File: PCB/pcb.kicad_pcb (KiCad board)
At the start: 2 copper layers, 116 x 75 mm, 174 parts, among them J1 EXT POWER, J2 TRACK POWER, J3 RJ45, J4 RJ45, J5 FROG0-1, J6 FROG2-3, J7 FROG4-5, J8 FROG6-7, K1 G6SK-2, K2 G6SK-2, K3 G6SK-2, K4 G6SK-2, K5 G6SK-2, K6 G6SK-2, K7 G6SK-2, K8 G6SK-2, M1 Motor_Servo, M2 Motor_Servo, M3 Motor_Servo, M4 Motor_Servo, M5 Motor_Servo, M6 Motor_Servo, M7 Motor_Servo, M8 Motor_Servo, Q1 MMBT2222A, Q10 MMBT2222A, Q11 MMBT2222A, Q12 MMBT2222A, Q13 MMBT2222A, Q14 MMBT2222A, Q15 MMBT2222A, Q16 MMBT2222A, Q2 MMBT2222A, Q3 MMBT2222A, Q4 MMBT2222A, Q5 MMBT2222A, Q6 MMBT2222A, Q7 MMBT2222A, Q8 MMBT2222A, Q9 MMBT2222A, SW2 Factory Reset, SW3 User, U2 PCA9685PW, U3 MCP23017_SO, U4 AP63205WU, U5 AP2114-3.3, U6 LM358, U7 TJA1051T-3, U8 MOUDLE-SEEEDUINO-XIAO-ESP32S3

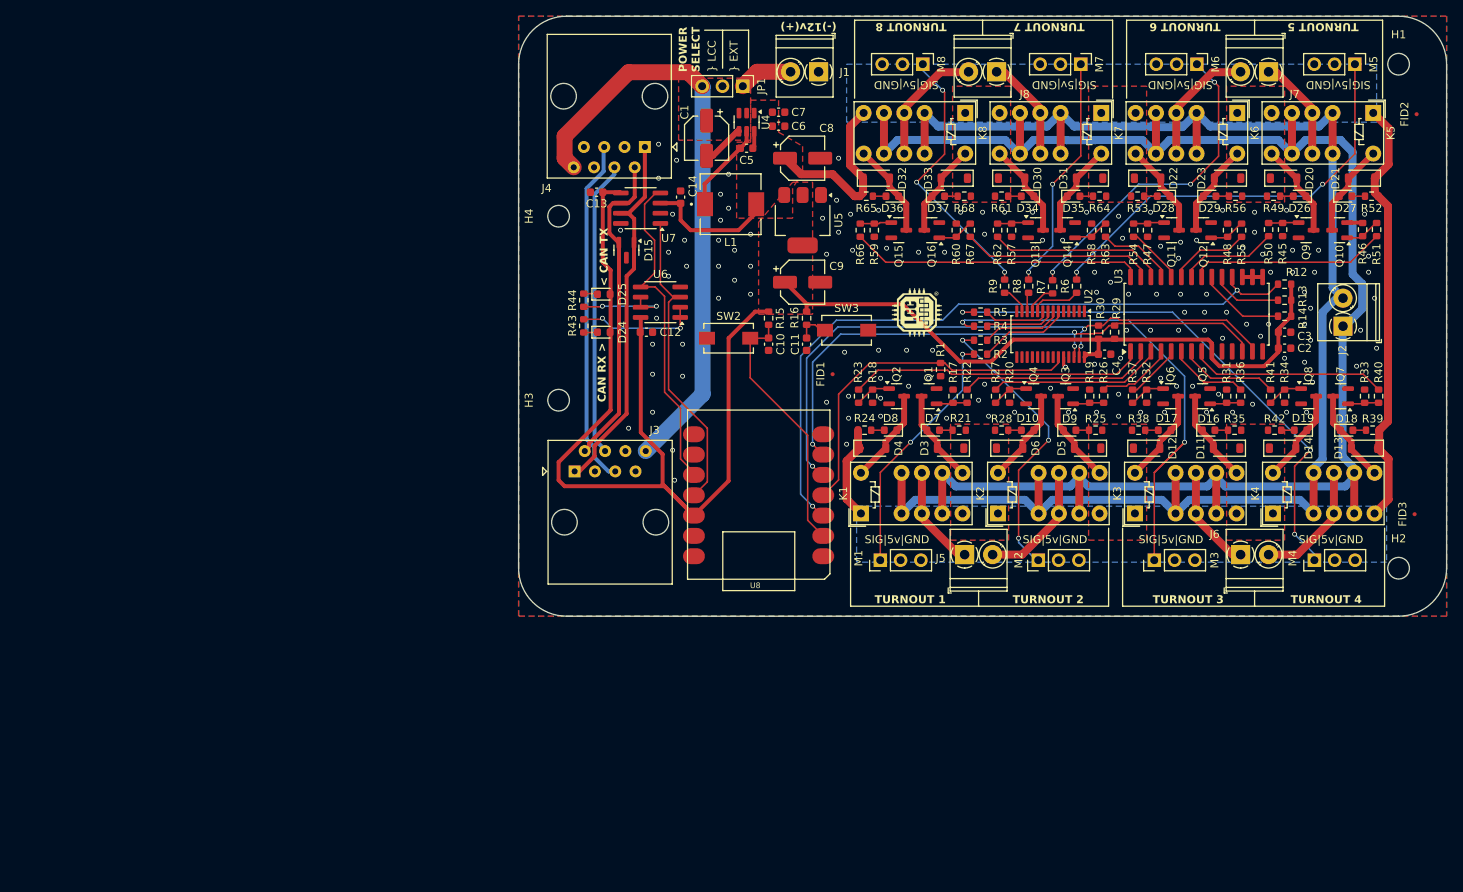
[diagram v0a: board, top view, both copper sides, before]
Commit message: Update with XIAO footprint
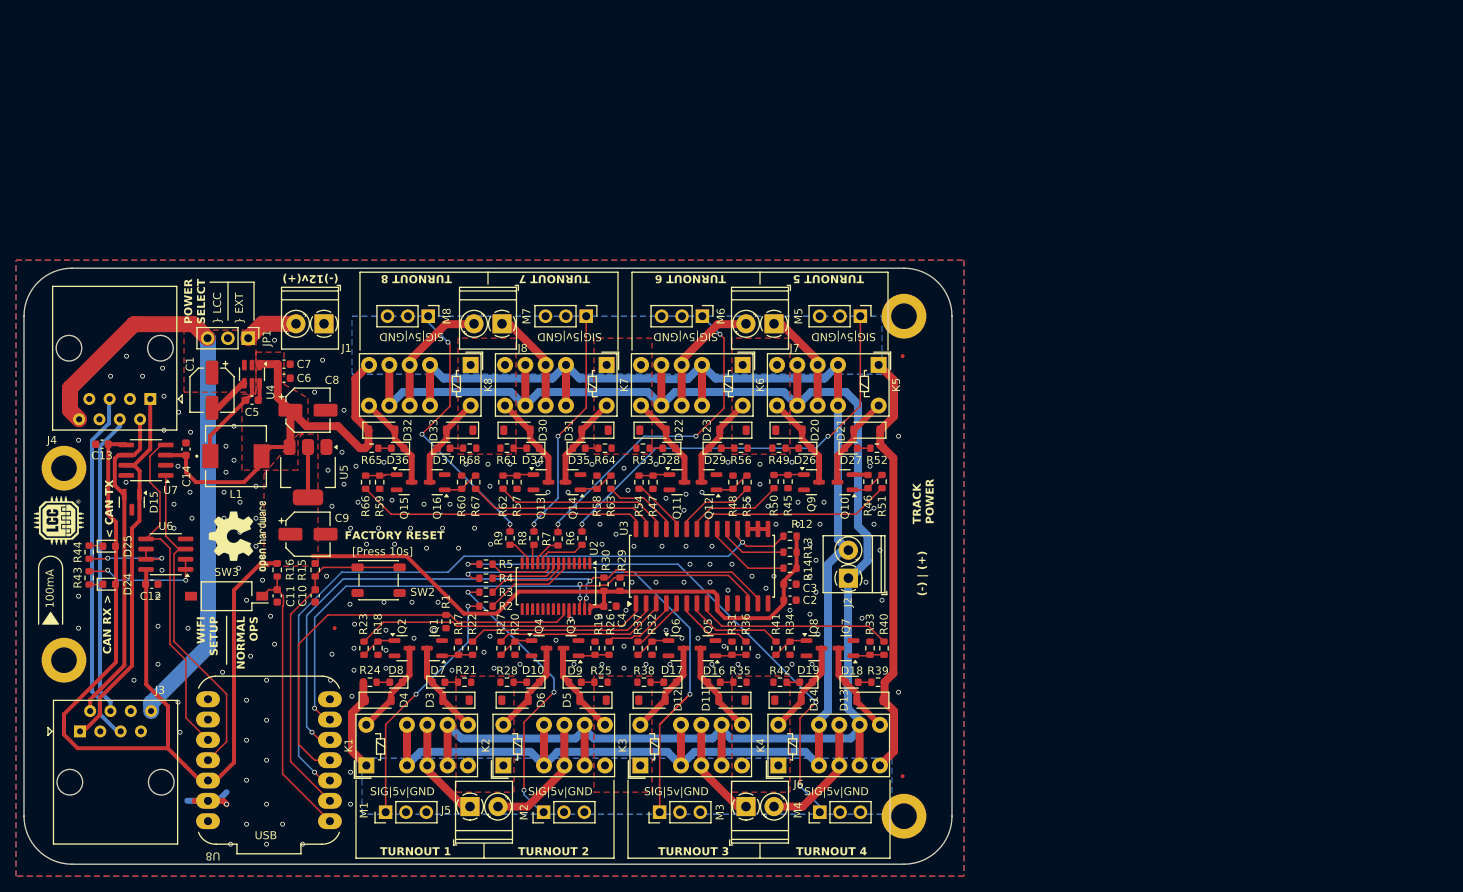
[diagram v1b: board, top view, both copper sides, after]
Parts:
- added REF**: OSHW-Logo2_9.8x8mm_SilkScreen, Symbol:OSHW-Logo2_9.8x8mm_SilkScreen, F.Cu at (106.0, 107.0)
- H1, H2, H3, H4: footprint MountingHole:MountingHole_2.7mm_M2.5 -> MountingHole:MountingHole_3.2mm_M3_DIN965_Pad
- SW2: footprint Button_Switch_SMD:SW_SPST_EVQPE1 -> Button_Switch_SMD:SW_SPST_PTS647_Sx50
- SW3: footprint Button_Switch_SMD:SW_SPST_EVQPE1 -> Button_Switch_SMD:SW_DIP_SPSTx01_Slide_Omron_A6S-110x_W8.9mm_P2.54mm
- U8: footprint xiao ESP32S3_PCB:MOUDLE14P-SMD-2.54-21X17.8MM -> CustomFootprints:MCU_Seeed_ESP32C3_TH
- moved G*** 110.4 mm to (83.5, 105.0)
- moved SW3 84.3 mm to (104.5, 114.5), turned to 180 degrees
- moved U8 82.6 mm to (109.8, 135.0)
- moved C11 73.3 mm to (110.8, 114.5)
- moved R16 73.3 mm to (110.8, 111.2)
- moved FID3 71.9 mm to (189.0, 137.0)
- moved FID2 71.0 mm to (189.0, 84.5)
- moved FID1 69.9 mm to (118.0, 118.5)
- moved H3 69.8 mm to (84.2, 122.5)
- moved J3 69.8 mm to (86.2, 131.4)
- moved D33 69.4 mm to (133.6, 93.8)
- moved D37 69.4 mm to (131.6, 96.0)
- moved J2 69.4 mm to (182.2, 112.2)
- moved K2 69.4 mm to (139.1, 135.7)
- moved K5 69.4 mm to (186.0, 85.6)
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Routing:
- net USER_BTN: track 4.26 -> 35.6 mm
- net +5V: track 106.2 -> 123.5 mm
- net FACTORY_RESET: track 32.2 -> 42.4 mm
- net GND: track 11.2 -> 20.7 mm, vias 136 -> 183
- net PWM_nENABLE: track 44.0 -> 53.4 mm
- net GPIO_nRESET: track 86.9 -> 89.8 mm
- net I2C_SDA: track 79.5 -> 82.4 mm
- net CAN-TX: track 39.3 -> 41.9 mm
- net I2C_SCL: track 73.2 -> 75.5 mm
- net CAN-RX: track 41.5 -> 43.5 mm
- net +3V3: track 202.1 -> 203.6 mm
- net ALT-A: track 37.0 -> 38.0 mm
- net VDDA: track 74.2 -> 75.2 mm
- net CAN-L: track 40.2 -> 41.2 mm
- net CAN-H: track 46.4 -> 47.3 mm
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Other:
- board size 116 x 75 mm -> 116 x 74.5 mm
- board text added: "(-) | (+)"
- board text added: "100mA"
- board text added: "FACTORY RESET"
- board text added: "NORMAL OPS"
- board text added: "TRACK POWER"
- board text added: "USB"
- board text added: "WIFI SETUP"
- board text added: "[Press 10s]"
- board text added: "https://github.com/vsi5004/LCCTurnoutController"

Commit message: Update project files
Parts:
- added D1: WiFi, LED_SMD:LED_0603_1608Metric, F.Cu at (107.8, 120.0)
- added D2: Activity, LED_SMD:LED_0603_1608Metric, F.Cu at (103.8, 120.0)
- added R10: 220R, Resistor_SMD:R_0603_1608Metric, F.Cu at (108.5, 122.5)
- added R11: 220R, Resistor_SMD:R_0603_1608Metric, F.Cu at (103.0, 122.5)
- H1, H2, H3, H4: footprint MountingHole:MountingHole_3.2mm_M3_DIN965_Pad -> MountingHole:MountingHole_3.2mm_M3_Pad
- SW2: footprint Button_Switch_SMD:SW_SPST_PTS647_Sx50 -> Button_Switch_SMD:SW_Tactile_SPST_NO_Straight_CK_PTS636Sx25SMTRLFS
- SW3: footprint Button_Switch_SMD:SW_DIP_SPSTx01_Slide_Omron_A6S-110x_W8.9mm_P2.54mm -> Button_Switch_SMD:SW_Tactile_SPST_NO_Straight_CK_PTS636Sx25SMTRLFS
- moved G*** 0.79 mm to (83.2, 105.8)
- moved SW2 0.79 mm to (122.8, 112.2)
- moved H3 0.72 mm to (83.5, 122.8)
- moved H4 0.67 mm to (83.5, 98.5)
- moved SW3 0.25 mm to (104.2, 114.5)
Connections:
- U8 pad 1: USER_BTN -> WIFI_LED
- U8 pad 10: CAN-RX -> CAN-TX
- U8 pad 11: CAN-TX -> ACTIVITY_LED
- U8 pad 2: FACTORY_RESET -> USER_BTN
- U8 pad 3: GPIO_nRESET -> FACTORY_RESET
- U8 pad 9: unconnected-(U8-PA7_A8_D8_SCK-Pad9) -> CAN-RX
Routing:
- net GPIO_nRESET: track 89.8 -> 8.59 mm, vias 2 -> 0
- net WIFI_LED: track 0.00 -> 23.6 mm
- net ACTIVITY_LED: track 0.00 -> 13.7 mm
- net FACTORY_RESET: track 42.4 -> 33.4 mm
- net +3V3: track 203.6 -> 206.1 mm
- net CAN-TX: track 41.9 -> 39.6 mm
- net CAN-RX: track 43.5 -> 41.6 mm
- net Net-(D2-K): track 0.00 -> 1.69 mm
- net Net-(D1-K): track 0.00 -> 1.69 mm
- net USER_BTN: track 35.6 -> 34.3 mm
- net I2C_SCL: track 75.5 -> 75.7 mm, vias 3 -> 2
- net I2C_SDA: vias 3 -> 2
- net GND: vias 183 -> 215
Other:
- board text added: "<WiFi"
- board text added: "Activity>"
- board text added: "USER"
- board text removed: "NORMAL OPS"
- board text removed: "WIFI SETUP"

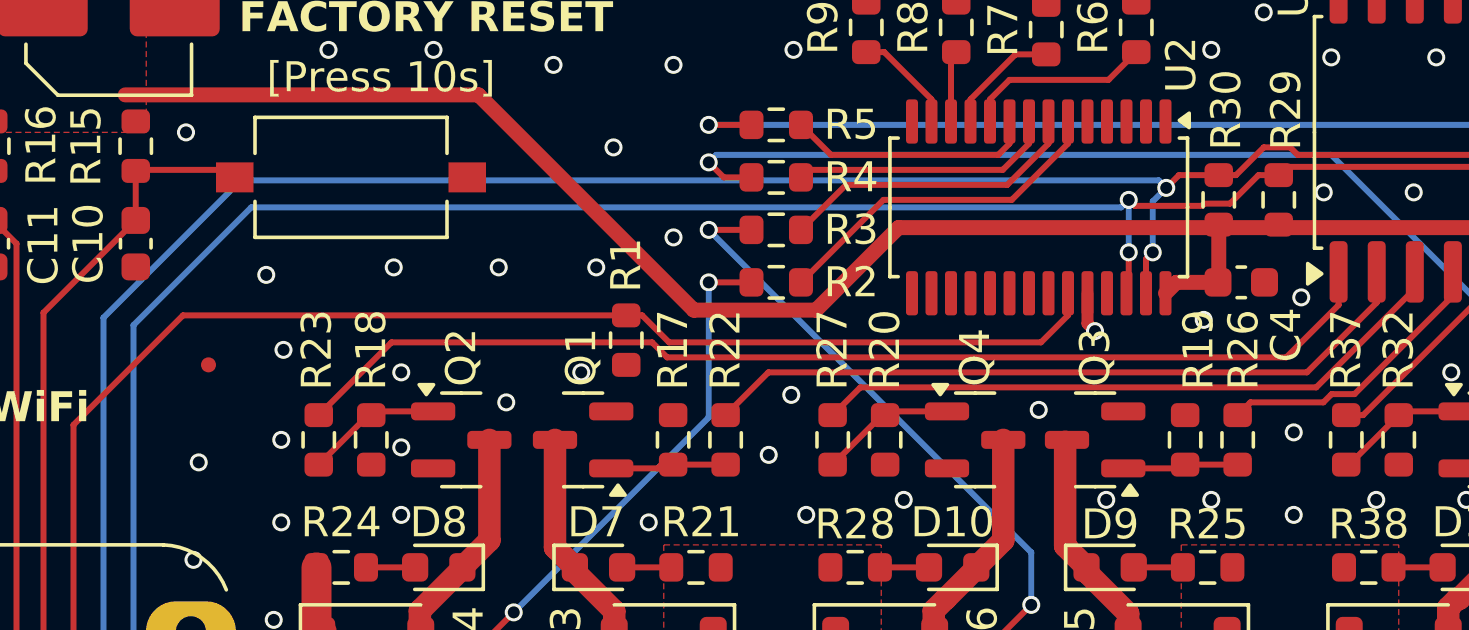
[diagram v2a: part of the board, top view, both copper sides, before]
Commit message: Fix live config updates not taking effect until reboot
ServoTurnout: preserve current state across ServoGPIOBit reconstruction
during runtime config changes. Previously, the placement-new reset
currentState_ to false, causing the first toggle to be silently eaten
(early return in set_state) and leaving the servo at stale endpoints.

Now saves the logical state before reconstruction and immediately
re-applies it via restore_state() with the new endpoint/frog values.
Also adds diagnostic logging to apply_configuration.

Includes PCB design updates.
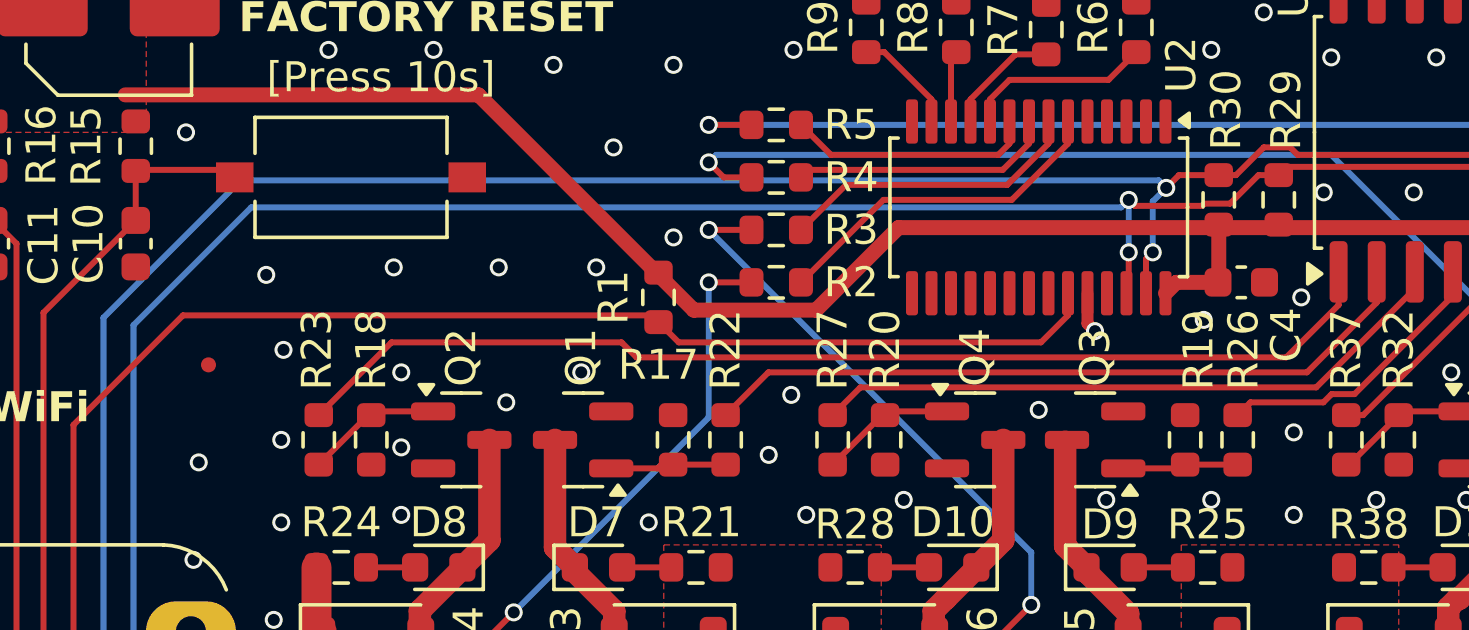
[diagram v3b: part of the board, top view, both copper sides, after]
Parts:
- moved R1 1.79 mm to (133.0, 116.2), turned to 90 degrees
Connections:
- R1 pad 2: GND -> +3V3
